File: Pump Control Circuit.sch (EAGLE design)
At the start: 25 parts, among them IC1 317T, IC2 LM555N, J1 POWER_JACKPTH, K1 351, Q1 BC548, Q2 BC548

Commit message: Add files via upload
I changed the relay on the board schematic to allow for more options and to also allow for relay sizes I believe to be more commonly available in Rwanda.
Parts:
- removed FRAME1: FRAME-LEDGER, SparkFun-Aesthetics:FRAME-LEDGER
- removed K1: 351, relay:351
- added K2: G2R2, relay:G2R2
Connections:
- removed net N$19: K12.P, ~2.1
- new net N$9: K22.P, ~2.1
- net N$13: now also K21.2; no longer K11.2
- net N$7: now also K22.S; no longer K12.S
- net V+: now also K21.1; no longer K11.1
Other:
- moved on the sheet: ~1, ~2
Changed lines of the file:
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@@
 <part name="D3" library="diode" deviceset="1N4004" device=""/>
 <part name="D4" library="diode" deviceset="1N4004" device=""/>
-<part name="FRAME1" library="SparkFun-Aesthetics" deviceset="FRAME-LEDGER" device=""/>
 <part name="J1" library="SparkFun-Connectors" deviceset="POWER_JACK" device="PTH"/>
 <part name="C3" library="SparkFun-Capacitors" deviceset="CAP_POL" device="PTH1"/>
@@
 <part name="Q1" library="transistor-npn" deviceset="BC548*" device=""/>
 <part name="Q2" library="transistor-npn" deviceset="BC548*" device=""/>
-<part name="K1" library="relay" deviceset="351" device=""/>
 <part name="GND5" library="SparkFun-Aesthetics" deviceset="GND" device=""/>
 <part name="GND6" library="SparkFun-Aesthetics" deviceset="GND" device=""/>
@@
 <part name="~1" library="SparkFun-Connectors" deviceset="M01" device="PTH"/>
 <part name="~2" library="SparkFun-Connectors" deviceset="M01" device="PTH"/>
+<part name="K2" library="relay" deviceset="G2R2" device=""/>
 </parts>
 <sheets>
@@
 <instance part="D3" gate="1" x="53.34" y="200.66"/>
 <instance part="D4" gate="1" x="45.72" y="208.28" rot="R90"/>
-<instance part="FRAME1" gate="G$1" x="-45.72" y="7.62"/>
-<instance part="FRAME1" gate="G$2" x="284.48" y="7.62"/>
 <instance part="J1" gate="G$1" x="15.24" y="208.28"/>
 <instance part="C3" gate="G$1" x="78.74" y="208.28"/>
@@
 <instance part="Q1" gate="G$1" x="144.78" y="114.3"/>
 <instance part="Q2" gate="G$1" x="60.96" y="101.6"/>
-<instance part="K1" gate="1" x="147.32" y="134.62"/>
-<instance part="K1" gate="2" x="198.12" y="154.94"/>
-<instance part="K1" gate="3" x="198.12" y="121.92"/>
 <instance part="GND5" gate="1" x="63.5" y="88.9"/>
 <instance part="GND6" gate="1" x="83.82" y="91.44"/>
@@
 <instance part="STOP" gate="G$1" x="50.8" y="68.58" rot="R90"/>
 <instance part="START" gate="G$1" x="76.2" y="127" rot="R270"/>
-<instance part="~1" gate="G$1" x="175.26" y="160.02"/>
-<instance part="~2" gate="G$1" x="198.12" y="139.7" rot="R90"/>
+<instance part="~1" gate="G$1" x="162.56" y="144.78"/>
+<instance part="~2" gate="G$1" x="180.34" y="127" rot="R90"/>
+<instance part="K2" gate="1" x="147.32" y="134.62"/>
+<instance part="K2" gate="2" x="180.34" y="139.7"/>
+<instance part="K2" gate="3" x="180.34" y="109.22"/>
 </instances>
 <busses>
@@
 <pinref part="D5" gate="1" pin="C"/>
 <wire x1="134.62" y1="137.16" x2="134.62" y2="147.32" width="0.1524" layer="91"/>
-<wire x1="134.62" y1="147.32" x2="147.32" y2="147.32" width="0.1524" layer="91"/>
-<pinref part="K1" gate="1" pin="1"/>
-<wire x1="147.32" y1="147.32" x2="147.32" y2="139.7" width="0.1524" layer="91"/>
 <wire x1="134.62" y1="147.32" x2="124.46" y2="147.32" width="0.1524" layer="91"/>
+<label x="124.46" y="147.32" size="1.778" layer="95"/>
+<pinref part="K2" gate="1" pin="1"/>
+<wire x1="147.32" y1="139.7" x2="147.32" y2="147.32" width="0.1524" layer="91"/>
+<wire x1="147.32" y1="147.32" x2="134.62" y2="147.32" width="0.1524" layer="91"/>
 <junction x="134.62" y="147.32"/>
-<label x="124.46" y="147.32" size="1.778" layer="95"/>
 </segment>
 <segment>
@@
 <segment>
 <pinref part="Q1" gate="G$1" pin="C"/>
-<pinref part="K1" gate="1" pin="2"/>
 <wire x1="147.32" y1="119.38" x2="147.32" y2="124.46" width="0.1524" layer="91"/>
 <wire x1="147.32" y1="124.46" x2="147.32" y2="129.54" width="0.1524" layer="91"/>
@@
 <junction x="147.32" y="124.46"/>
 <pinref part="D5" gate="1" pin="A"/>
+<pinref part="K2" gate="1" pin="2"/>
 </segment>
 </net>
@@
 </segment>
 </net>
-<net name="N$19" class="0">
+<net name="N$7" class="0">
+<segment>
+<pinref part="~1" gate="G$1" pin="1"/>
+<pinref part="K2" gate="2" pin="S"/>
+<wire x1="170.18" y1="144.78" x2="175.26" y2="144.78" width="0.1524" layer="91"/>
+</segment>
+</net>
+<net name="N$9" class="0">
 <segment>
 <pinref part="~2" gate="G$1" pin="1"/>
-<pinref part="K1" gate="2" pin="P"/>
-<wire x1="198.12" y1="147.32" x2="198.12" y2="152.4" width="0.1524" layer="91"/>
-</segment>
-</net>
-<net name="N$7" class="0">
-<segment>
-<pinref part="K1" gate="2" pin="S"/>
-<pinref part="~1" gate="G$1" pin="1"/>
-<wire x1="193.04" y1="160.02" x2="182.88" y2="160.02" width="0.1524" layer="91"/>
-</segment>
-</net>
+<pinref part="K2" gate="2" pin="P"/>
+<wire x1="180.34" y1="134.62" x2="180.34" y2="137.16" width="0.1524" layer="91"/>
+</segment>
+</net>

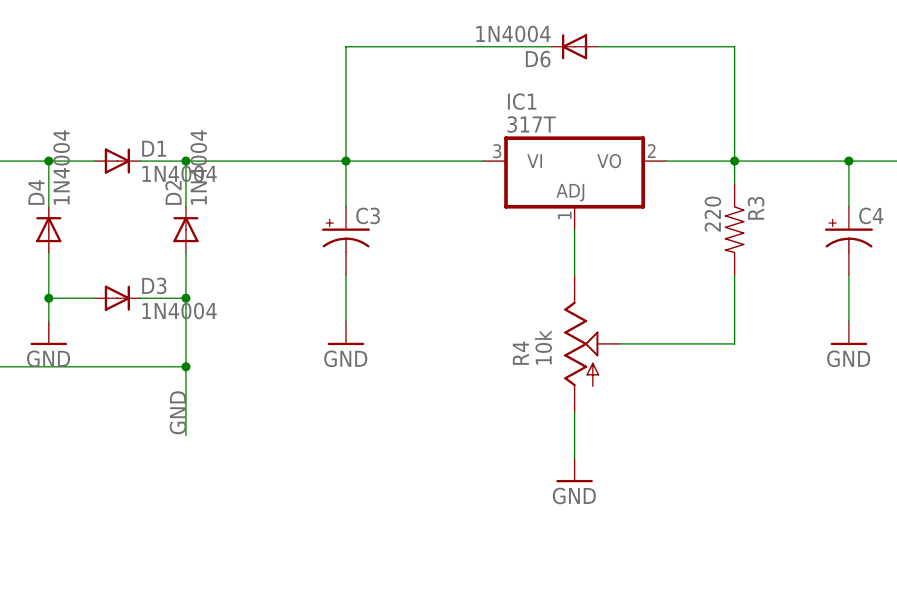
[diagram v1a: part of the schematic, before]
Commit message: Add files via upload
Fixed the voltage regulator footprint to not be intersecting with the relay footprint
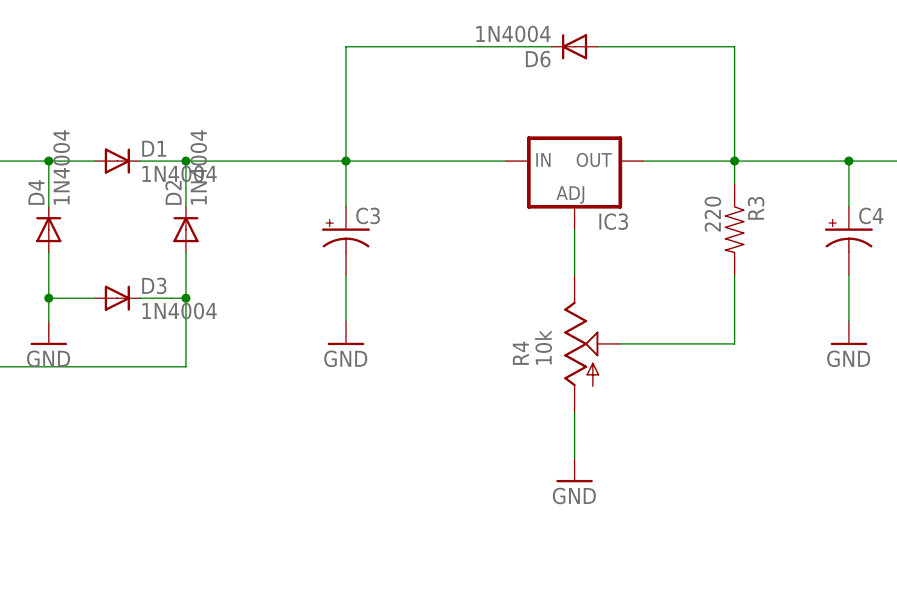
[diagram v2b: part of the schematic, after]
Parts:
- removed IC1: 317T, linear:317T
- added IC3: (no value), v-reg:LM317TS
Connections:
- new net NEUTRAL: D2.A, D3.C, J1.GND, J1.GNDBREAK
- net GND: no longer D2.A, D3.C, J1.GND, J1.GNDBREAK
- net N$1: now also IC3.ADJ; no longer IC1.ADJ
- net N$8: now also IC3.IN; no longer IC1.VI
- net V+: now also IC3.OUT; no longer IC1.VO
